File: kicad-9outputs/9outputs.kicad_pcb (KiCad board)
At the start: 2 copper layers, 57.6 x 81.1 mm, 20 parts, among them J1 Screw_Terminal_01x04, J11 Screw_Terminal_01x02, J2 Screw_Terminal_01x04, J3 Screw_Terminal_01x04, J4 Screw_Terminal_01x03, Q1 BSP75N, Q2 BSP75N, Q3 BSP75N, Q4 BSP75N, Q5 BSP75N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

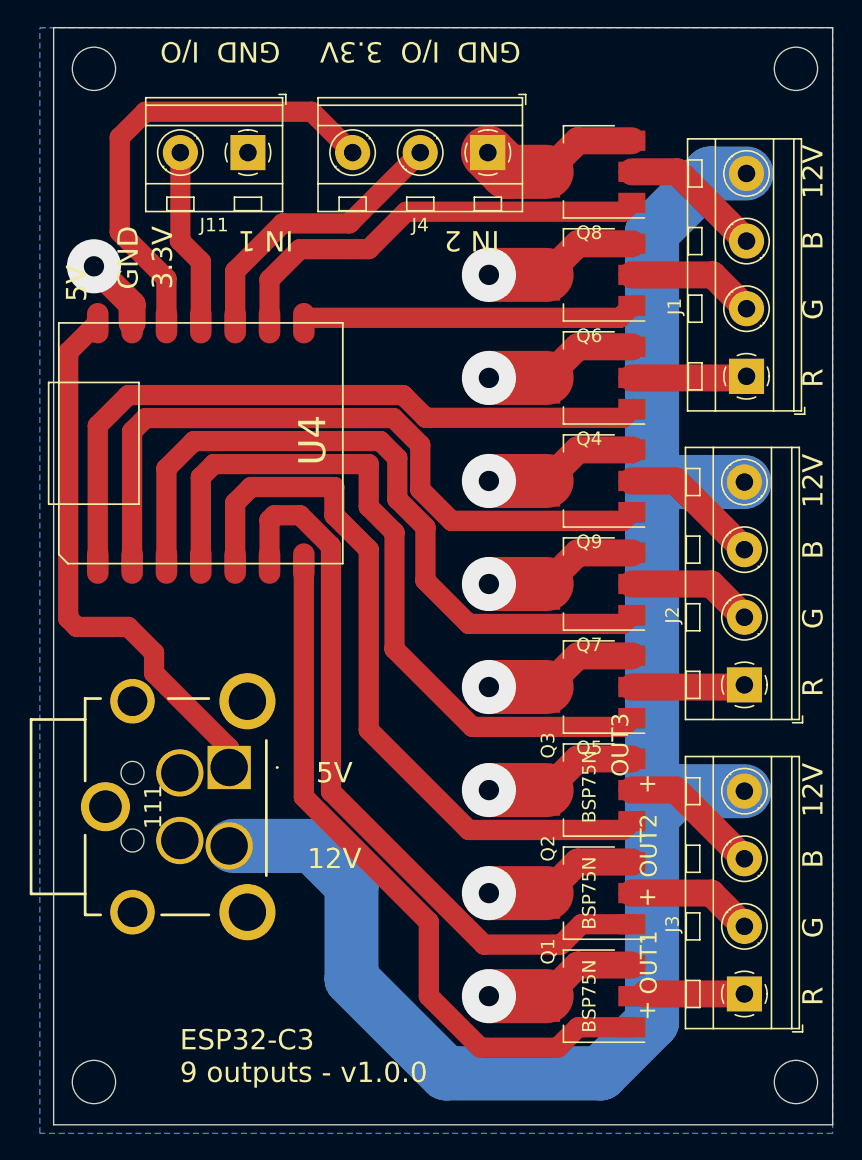
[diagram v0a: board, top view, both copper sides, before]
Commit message: feat: add 5 outputs
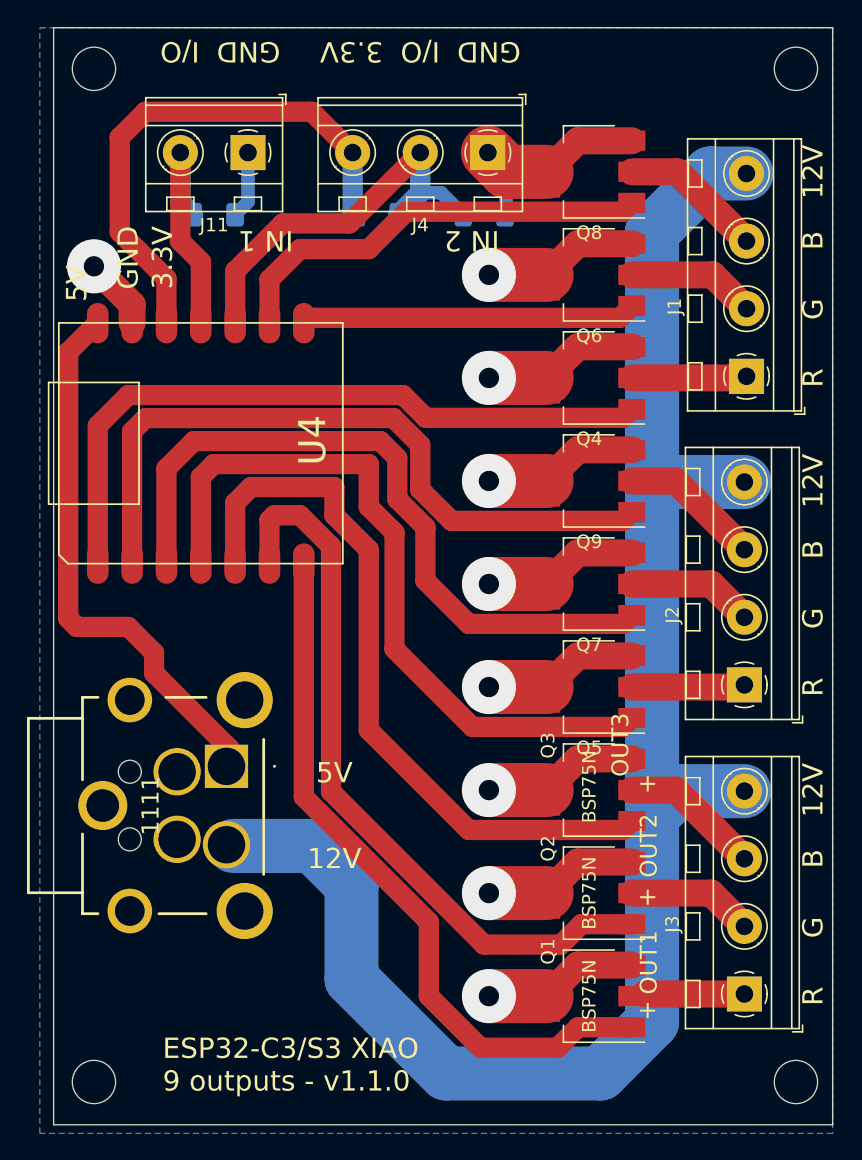
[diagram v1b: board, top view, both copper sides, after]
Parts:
- removed 111: KPJX-4S-S, kpjx:KPJX4SS
- added 1111: KPJX-4S-S, custom2:KPJX4SS, F.Cu at (103.5, 87.4)
- added R1: R, Resistor_SMD:R_1206_3216Metric_Pad1.30x1.75mm_HandSolder, B.Cu at (102.6, 46.6)
- added R2: R, Resistor_SMD:R_1206_3216Metric_Pad1.30x1.75mm_HandSolder, B.Cu at (114.7, 46.6)
- added R3: R, Resistor_SMD:R_1206_3216Metric_Pad1.30x1.75mm_HandSolder, B.Cu at (122.6, 46.6)
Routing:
- net GND: track 109.7 -> 120.3 mm
- net IN2: track 21.2 -> 30.3 mm
- net IN1: track 13.3 -> 18.3 mm
- net +3.3V: track 34.4 -> 39.1 mm
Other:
- board text added: "ESP32-C3/S3 XIAO 9 outputs - v1.1.0"
- board text removed: "ESP32-C3 9 outputs - v1.0.0"
